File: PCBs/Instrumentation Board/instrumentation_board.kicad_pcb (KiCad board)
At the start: 2 copper layers, 54 parts, among them J1 Conn_01x02, J2 Conn_01x02, J3 Conn_01x02, J4 Conn_01x02, J5 Conn_01x02, Q1 TEMT6000X01, U1 GPS-ADAFRUIT746, U10 PI4ULS5V201TAEX, U11 PI4ULS5V201TAEX, U12 PI4ULS5V201TAEX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

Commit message: finished traces on instr board
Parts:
- removed C4, C5: 100nF, Capacitors_SMD:C_0805_HandSoldering
- moved J2 137.3 mm to (140.0, 136.7)
- moved J3 121.2 mm to (133.6, 136.7)
- moved J1 118.5 mm to (114.3, 136.7)
- moved J5 113.9 mm to (120.9, 136.7)
- moved J4 113.8 mm to (127.3, 136.7)
- moved U3 33.5 mm to (144.3, 125.2)
- moved C2 26.9 mm to (148.6, 125.5), turned to 270 degrees
- moved C1 1.30 mm to (148.6, 120.1), turned to 270 degrees
- moved C20 0.25 mm to (114.8, 114.8)
- moved C21 0.25 mm to (112.8, 114.8)
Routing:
- net 1.8V: track 30.0 -> 178.7 mm, vias 0 -> 10
- net 7.4V: track 12.5 -> 100.9 mm
- net INT1_1.8V: track 0.00 -> 73.9 mm, vias 0 -> 3
- net 5V: track 26.1 -> 96.5 mm, vias 0 -> 8
- net INT0_1.8V: track 0.00 -> 64.4 mm, vias 0 -> 3
- net SCL_1.8V: track 0.00 -> 51.2 mm, vias 0 -> 3
- net SDA_1.8V: track 0.00 -> 47.0 mm, vias 0 -> 3
- net SCL_5V: track 9.66 -> 54.0 mm, vias 1 -> 2
- net SDA_5V: track 4.43 -> 47.7 mm, vias 0 -> 2
- net GND: track 62.8 -> 105.7 mm, vias 15 -> 24
- net /Sheet5ABF9899_3/THERM_OUT: track 3.66 -> 38.4 mm, vias 0 -> 1
- net /Sheet5ABF9899/THERM_OUT: track 3.66 -> 29.7 mm, vias 0 -> 1
- net /Sheet5ABF9899_2/THERM_OUT: track 3.66 -> 26.1 mm, vias 0 -> 1
- net +5V: track 27.4 -> 5.08 mm, vias 3 -> 0
- net 3V: track 77.3 -> 88.9 mm, vias 5 -> 7
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- added copper zone on F.Cu, net 5V
- added copper zone on B.Cu, net GND
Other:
- net class Default: clearance 0.2 -> 0.127
- rule trace_clearance: 0.2 -> 0.127

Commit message: edge cuts and screw holes
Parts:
- added REF**: MountingHole_3.2mm_M3, Mounting_Holes:MountingHole_3.2mm_M3, F.Cu at (66.0, 78.7)
- added REF**: MountingHole_3.2mm_M3, Mounting_Holes:MountingHole_3.2mm_M3, F.Cu at (66.0, 134.6)
- added REF**: MountingHole_3.2mm_M3, Mounting_Holes:MountingHole_3.2mm_M3, F.Cu at (149.9, 134.6)
- added REF**: MountingHole_3.2mm_M3, Mounting_Holes:MountingHole_3.2mm_M3, F.Cu at (149.9, 78.7)
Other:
- board outline added: 91.4 x 63.5 mm
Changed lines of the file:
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@@
     (links 149)
     (no_connects 0)
-    (area 69.139999 79.741 153.924001 147)
+    (area 62.154999 77.394999 161.365001 138.505001)
     (thickness 1.6)
-    (drawings 0)
-    (tracks 666)
+    (drawings 6)
+    (tracks 667)
     (zones 0)
-    (modules 52)
+    (modules 56)
     (nets 60)
   )
@@
     (add_net SS)
   )
+  (module Mounting_Holes:MountingHole_3.2mm_M3 (layer F.Cu)
+    (at 66.04 78.74)
+    (descr "Mounting Hole 3.2mm, no annular, M3")
+    (tags "mounting hole 3.2mm no annular m3")
+    (attr virtual)
+    (fp_text reference REF** (at 0 -4.2) (layer F.SilkS) hide
+      (effects (font (size 1 1) (thickness 0.15)))
+    )
+    (fp_text value MountingHole_3.2mm_M3 (at 0 4.2) (layer F.Fab) hide
+      (effects (font (size 1 1) (thickness 0.15)))
+    )
+    (fp_text user %R (at 0.3 0) (layer F.Fab)
+      (effects (font (size 1 1) (thickness 0.15)))
+    )
+    (fp_circle (center 0 0) (end 3.2 0) (layer Cmts.User) (width 0.15))
+    (fp_circle (center 0 0) (end 3.45 0) (layer F.CrtYd) (width 0.05))
+    (pad 1 np_thru_hole circle (at 0 0) (size 3.2 3.2) (drill 3.2) (layers *.Cu *.Mask))
+  )
+  (module Mounting_Holes:MountingHole_3.2mm_M3 (layer F.Cu)
+    (at 66.04 134.62)
+    (descr "Mounting Hole 3.2mm, no annular, M3")
+    (tags "mounting hole 3.2mm no annular m3")
+    (attr virtual)
+    (fp_text reference REF** (at 0 -4.2) (layer F.SilkS) hide
+      (effects (font (size 1 1) (thickness 0.15)))
+    )
+    (fp_text value MountingHole_3.2mm_M3 (at 0 4.2) (layer F.Fab) hide
+      (effects (font (size 1 1) (thickness 0.15)))
+    )
+    (fp_text user %R (at 0.3 0) (layer F.Fab)
+      (effects (font (size 1 1) (thickness 0.15)))
+    )
+    (fp_circle (center 0 0) (end 3.2 0) (layer Cmts.User) (width 0.15))
+    (fp_circle (center 0 0) (end 3.45 0) (layer F.CrtYd) (width 0.05))
+    (pad 1 np_thru_hole circle (at 0 0) (size 3.2 3.2) (drill 3.2) (layers *.Cu *.Mask))
+  )
+  (module Mounting_Holes:MountingHole_3.2mm_M3 (layer F.Cu)
+    (at 149.86 134.62)
+    (descr "Mounting Hole 3.2mm, no annular, M3")
+    (tags "mounting hole 3.2mm no annular m3")
+    (attr virtual)
+    (fp_text reference REF** (at 0 -4.2) (layer F.SilkS) hide
+      (effects (font (size 1 1) (thickness 0.15)))
+    )
+    (fp_text value MountingHole_3.2mm_M3 (at 0 4.2) (layer F.Fab) hide
+      (effects (font (size 1 1) (thickness 0.15)))
+    )
+    (fp_text user %R (at 0.3 0) (layer F.Fab)
+      (effects (font (size 1 1) (thickness 0.15)))
+    )
+    (fp_circle (center 0 0) (end 3.2 0) (layer Cmts.User) (width 0.15))
+    (fp_circle (center 0 0) (end 3.45 0) (layer F.CrtYd) (width 0.05))
+    (pad 1 np_thru_hole circle (at 0 0) (size 3.2 3.2) (drill 3.2) (layers *.Cu *.Mask))
+  )
+  (module Mounting_Holes:MountingHole_3.2mm_M3 (layer F.Cu)
+    (at 149.86 78.74)
+    (descr "Mounting Hole 3.2mm, no annular, M3")
+    (tags "mounting hole 3.2mm no annular m3")
+    (attr virtual)
+    (fp_text reference REF** (at 0 -4.2) (layer F.SilkS) hide
+      (effects (font (size 1 1) (thickness 0.15)))
+    )
+    (fp_text value MountingHole_3.2mm_M3 (at 0 4.2) (layer F.Fab) hide
+      (effects (font (size 1 1) (thickness 0.15)))
+    )
+    (fp_text user %R (at 0.3 0) (layer F.Fab)
+      (effects (font (size 1 1) (thickness 0.15)))
+    )
+    (fp_circle (center 0 0) (end 3.2 0) (layer Cmts.User) (width 0.15))
+    (fp_circle (center 0 0) (end 3.45 0) (layer F.CrtYd) (width 0.05))
+    (pad 1 np_thru_hole circle (at 0 0) (size 3.2 3.2) (drill 3.2) (layers *.Cu *.Mask))
+  )
   (module arduino:Arduino_Nano (layer F.Cu)
     (at 119.253 88.265)
     (descr "Arduino Nano, http://www.mouser.com/pdfdocs/Gravitech_Arduino_Nano3_0.pdf")
     (tags "Arduino Nano")
-    (fp_text reference A1 (at 7.62 43.18) (layer F.SilkS)
-      (effects (font (size 1 1) (thickness 0.15)))
-    )
-    (fp_text value Arduino_Nano (at 8.89 19.05 90) (layer F.Fab)
+    (fp_text reference A1 (at 8.001 -2.667) (layer F.SilkS)
+      (effects (font (size 1 1) (thickness 0.15)))
+    )
+    (fp_text value Arduino_Nano (at 8.89 19.05 90) (layer F.Fab) hide
       (effects (font (size 1 1) (thickness 0.15)))
     )
@@
     (tags "capacitor 0805")
     (attr smd)
-    (fp_text reference C1 (at 3.556 0 270) (layer F.SilkS)
+    (fp_text reference C1 (at 0 -2.032 360) (layer F.SilkS)
       (effects (font (size 1 1) (thickness 0.15)))
     )
@@
     (tags "capacitor 0805")
     (attr smd)
-    (fp_text reference C2 (at 3.302 0.1016 270) (layer F.SilkS)
+    (fp_text reference C2 (at 0 -2.032 360) (layer F.SilkS)
       (effects (font (size 1 1) (thickness 0.15)))
     )
@@
   (module adafruit:gps746 (layer F.Cu)
     (at 103.378 97.028 90)
-    (fp_text reference U1 (at 0 -17.28 90) (layer F.SilkS)
-      (effects (font (size 1 1) (thickness 0.15)))
-    )
-    (fp_text value GPS-ADAFRUIT746 (at 0 -18.28 90) (layer F.Fab)
+    (fp_text reference U1 (at 12.446 1.27 180) (layer F.SilkS)
+      (effects (font (size 1 1) (thickness 0.15)))
+    )
+    (fp_text value GPS-ADAFRUIT746 (at 0 -18.28 90) (layer F.Fab) hide
       (effects (font (size 1 1) (thickness 0.15)))
     )
@@
   (module adafruit:adafruit254 (layer F.Cu)
     (at 87.63 136.398)
-    (fp_text reference U5 (at 6.4 9.6) (layer F.SilkS)
-      (effects (font (size 1 1) (thickness 0.15)))
-    )
-    (fp_text value MicroSD-ADAFRUIT254 (at -7.62 -5.08) (layer F.Fab)
+    (fp_text reference U5 (at 17.018 -0.762) (layer F.SilkS)
+      (effects (font (size 1 1) (thickness 0.15)))
+    )
+    (fp_text value MicroSD-ADAFRUIT254 (at -7.62 -5.08) (layer F.Fab) hide
       (effects (font (size 1 1) (thickness 0.15)))
     )
@@
     (tags SOT-23-5)
     (attr smd)
-    (fp_text reference U6 (at 0 -2.9 270) (layer F.SilkS)
+    (fp_text reference U6 (at 0 -2.794 360) (layer F.SilkS)
       (effects (font (size 1 1) (thickness 0.15)))
     )
@@
     )
   )
+  (gr_line (start 153.67 74.93) (end 66.04 74.93) (angle 90) (layer Edge.Cuts) (width 0.15))
+  (gr_line (start 153.67 138.43) (end 62.23 138.43) (angle 90) (layer Edge.Cuts) (width 0.15))
+  (gr_line (start 153.67 74.93) (end 153.67 138.43) (angle 90) (layer Edge.Cuts) (width 0.15))
+  (gr_line (start 62.23 74.93) (end 66.04 74.93) (angle 90) (layer Edge.Cuts) (width 0.15))
+  (gr_line (start 62.23 77.47) (end 62.23 74.93) (angle 90) (layer Edge.Cuts) (width 0.15))
+  (gr_line (start 62.23 138.43) (end 62.23 77.47) (angle 90) (layer Edge.Cuts) (width 0.15))
   (segment (start 101.346 99.568) (end 104.14 99.568) (width 0.25) (layer B.Cu) (net 1) (status 10))
   (via (at 104.902 88.392) (size 0.6) (drill 0.4) (layers F.Cu B.Cu) (net 1))
@@
   (segment (start 134.62 113.792) (end 134.493 113.665) (width 0.25) (layer F.Cu) (net 8) (status 30))
   (segment (start 119.253 98.425) (end 115.015 98.425) (width 0.25) (layer F.Cu) (net 9))
+  (segment (start 131.572 126.238) (end 131.572 125.73) (width 0.25) (layer B.Cu) (net 10))
+  (segment (start 131.572 125.73) (end 131.826 125.476) (width 0.25) (layer B.Cu) (net 10))
   (segment (start 128.524 133.604) (end 128.524 129.54) (width 0.25) (layer F.Cu) (net 10))
   (segment (start 132.715 111.125) (end 134.493 111.125) (width 0.25) (layer B.Cu) (net 10))
   (segment (start 131.826 112.014) (end 132.715 111.125) (width 0.25) (layer B.Cu) (net 10))
-  (segment (start 131.826 126.238) (end 131.826 112.014) (width 0.25) (layer B.Cu) (net 10))
-  (segment (start 131.572 126.238) (end 131.826 126.238) (width 0.25) (layer B.Cu) (net 10))
+  (segment (start 131.826 125.476) (end 131.826 112.014) (width 0.25) (layer B.Cu) (net 10))
   (via (at 131.572 126.238) (size 0.6) (drill 0.4) (layers F.Cu B.Cu) (net 10))
   (segment (start 128.524 129.54) (end 131.572 126.238) (width 0.25) (layer F.Cu) (net 10))
@@
   (segment (start 137.969 108.585) (end 138.096 108.712) (width 0.25) (layer F.Cu) (net 12))
   (segment (start 115.015 103.505) (end 119.253 103.505) (width 0.25) (layer F.Cu) (net 13) (status 20))
-  (segment (start 113.03 133.604) (end 113.792 133.604) (width 0.25) (layer F.Cu) (net 14))
-  (segment (start 113.792 133.604) (end 120.396 127) (width 0.25) (layer F.Cu) (net 14))
+  (segment (start 120.65 127) (end 119.634 127) (width 0.25) (layer F.Cu) (net 14))
+  (segment (start 119.634 127) (end 113.03 133.604) (width 0.25) (layer F.Cu) (net 14))
   (segment (start 120.396 127) (end 120.65 127) (width 0.25) (layer F.Cu) (net 14))
   (via (at 120.65 127) (size 0.6) (drill 0.4) (layers F.Cu B.Cu) (net 14))

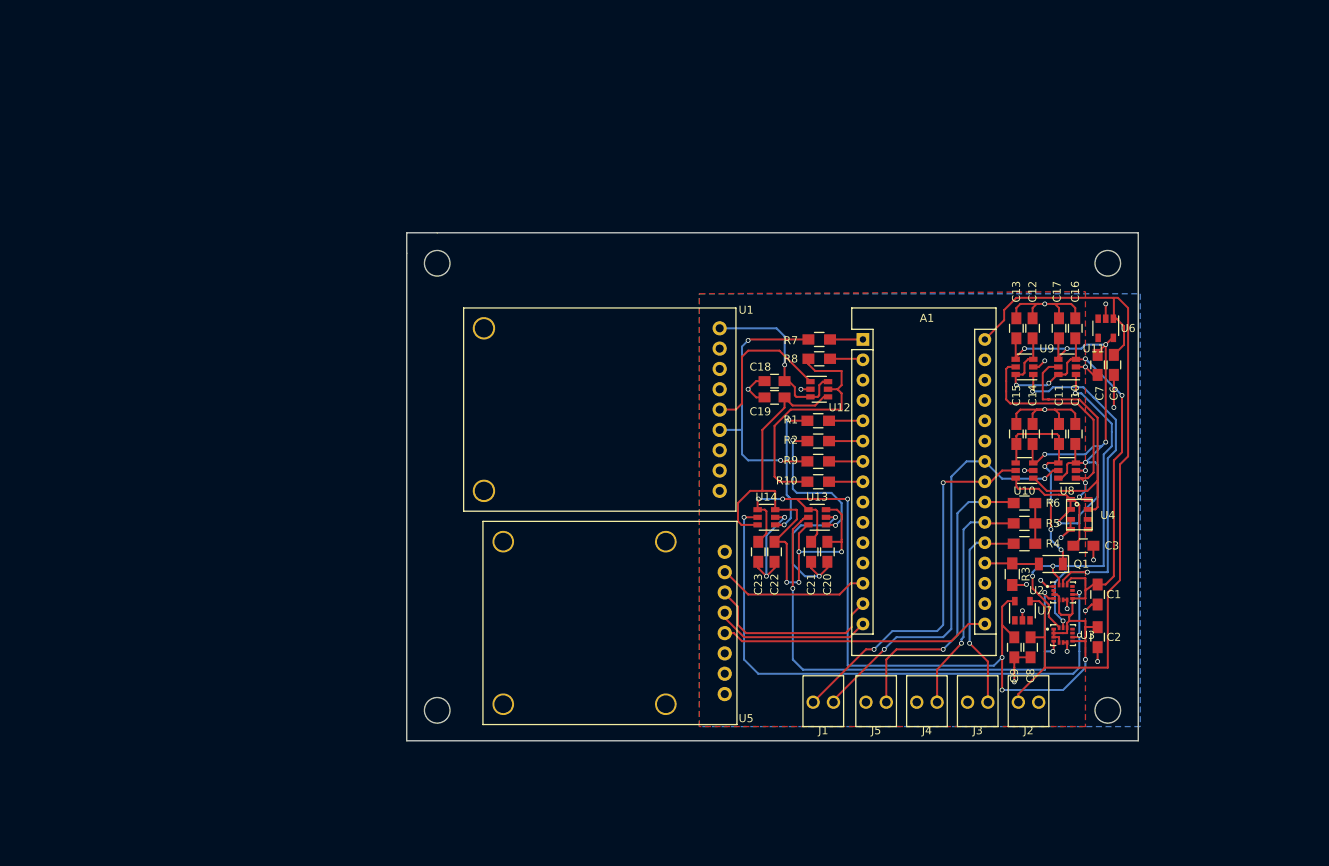
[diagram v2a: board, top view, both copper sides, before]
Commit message: rerouted payload instr board and completed all changes per Alexs review
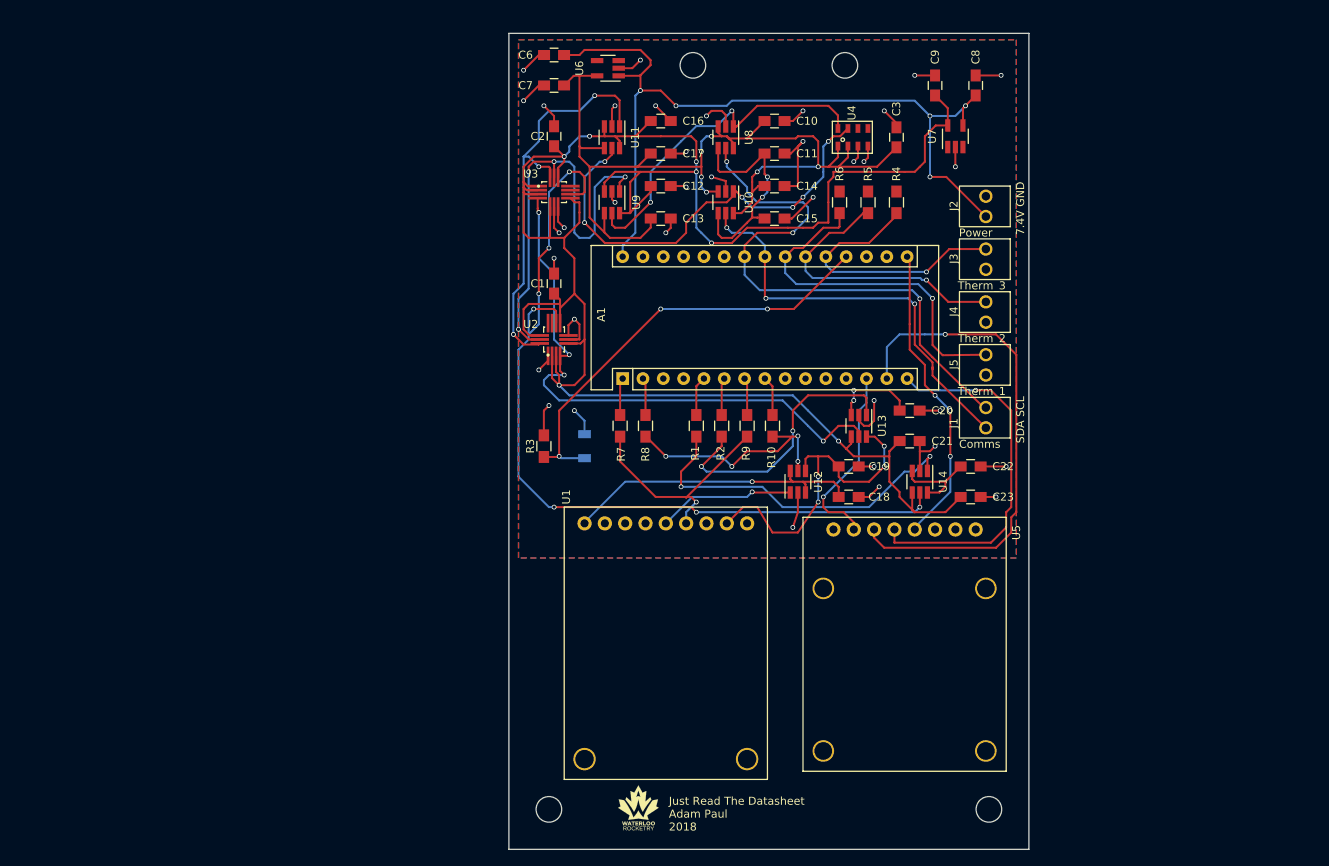
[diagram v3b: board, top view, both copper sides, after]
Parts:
- added G***: LOGO, Logos:logo6, F.Cu at (91.2, 146.8)
- Q1: moved to B.Cu
- U10, U11, U12, U13, U14, U8, U9: footprint sot:SOT-23-6 -> TO_SOT_Packages_SMD:SOT-23-6_Handsoldering
- U2, U3: footprint lga:LGA-14 -> LGA_Long:LGA-14
- U6, U7: footprint sot:SOT-23-5 -> TO_SOT_Packages_SMD:SOT-23-5_HandSoldering
- moved REF** 95.9 mm to (98.0, 54.0), turned to 90 degrees
- moved C2 92.4 mm to (80.6, 62.9), turned to 90 degrees
- moved U3 84.3 mm to (80.6, 69.8)
- moved C6 80.0 mm to (80.6, 52.7), turned to 180 degrees
- moved C1 78.3 mm to (80.6, 81.3), turned to 90 degrees
- moved C7 76.4 mm to (80.6, 56.5), turned to 180 degrees
- moved U2 71.1 mm to (80.6, 88.3), turned to 90 degrees
- moved C9 70.9 mm to (128.3, 56.5), turned to 90 degrees
- moved C8 70.6 mm to (133.3, 56.5), turned to 90 degrees
- moved U6 70.2 mm to (87.4, 54.4), turned to 180 degrees
- moved REF** 70.1 mm to (135.0, 147.0), turned to 90 degrees
- moved REF** 69.7 mm to (80.0, 147.0), turned to 90 degrees
- moved J2 65.1 mm to (137.7, 71.6), turned to 90 degrees
- moved U11 63.7 mm to (87.9, 63.0), turned to 270 degrees
- moved R3 60.7 mm to (79.4, 101.6), turned to 90 degrees
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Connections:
- R4 pad 1: +5V -> 5V
- R5 pad 1: +5V -> 5V
- R6 pad 1: +5V -> 5V
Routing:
- net 1.8V: track 178.7 -> 263.1 mm, vias 10 -> 7
- net SIG: track 6.81 -> 54.8 mm, vias 0 -> 3
- net MOSI: track 23.3 -> 63.8 mm, vias 0 -> 1
- net INT1_1.8V: track 73.9 -> 108.6 mm, vias 3 -> 7
- net 3V: track 88.9 -> 122.3 mm, vias 7 -> 6
- net MISO: track 19.6 -> 46.0 mm, vias 0 -> 1
- net INT1_5V: track 19.1 -> 43.8 mm
- net SDA_3V: track 35.2 -> 55.9 mm, vias 0 -> 6
- net SCL_5V: track 54.0 -> 70.0 mm, vias 2 -> 3
- net /ICShifter7/VccA: track 22.5 -> 38.5 mm
- net INT0_5V: track 19.1 -> 34.5 mm
- net SCL_3V: track 30.9 -> 43.2 mm
- net GND: track 105.7 -> 117.4 mm, vias 24 -> 35
- net INT0_1.8V: track 64.4 -> 72.5 mm, vias 3 -> 4
- net /Sheet5ABF9899_2/THERM_OUT: track 26.1 -> 34.2 mm
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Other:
- board size 91.4 x 63.5 mm -> 65 x 102 mm
- rule pad_to_mask_clearance: 0.2 -> 0.002
- board text added: "7.4V GND"
- board text added: "Comms"
- board text added: "Just Read The Datasheet Adam Paul 2018"
- board text added: "Power"
- board text added: "SDA SCL"
- board text added: "Therm_1"
- board text added: "Therm_2"
- board text added: "Therm_3"
